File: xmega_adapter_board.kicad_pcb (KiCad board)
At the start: 2 copper layers, 31 x 72.4 mm, 17 parts, among them J1 Conn_01x04, J2 Conn_01x08, J3 Conn_01x08, J4 Conn_01x04, J5 Conn_01x08, J6 Conn_01x08, J7 Conn_01x08, J8 Conn_01x08, U1 ATxmega256D3-AU

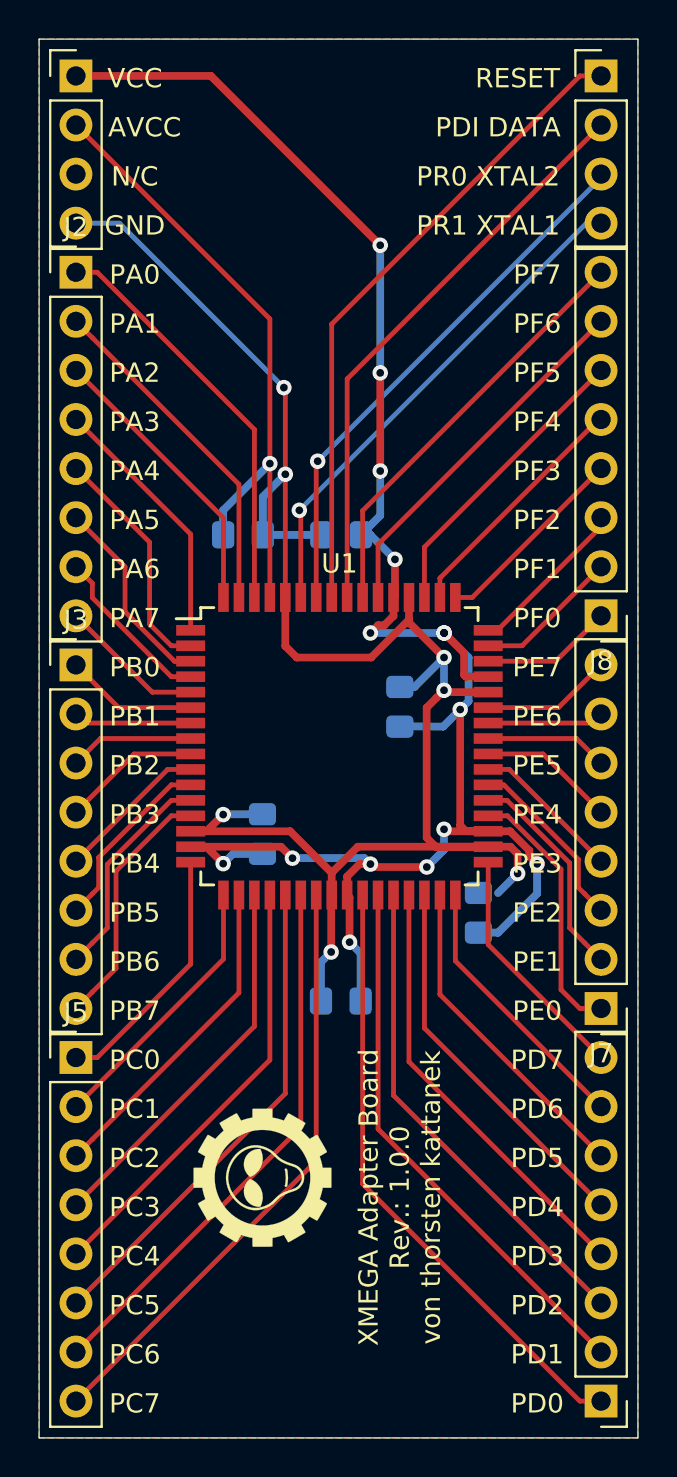
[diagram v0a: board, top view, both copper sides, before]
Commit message: Power LED als rote SMD LED hinzugefuegt
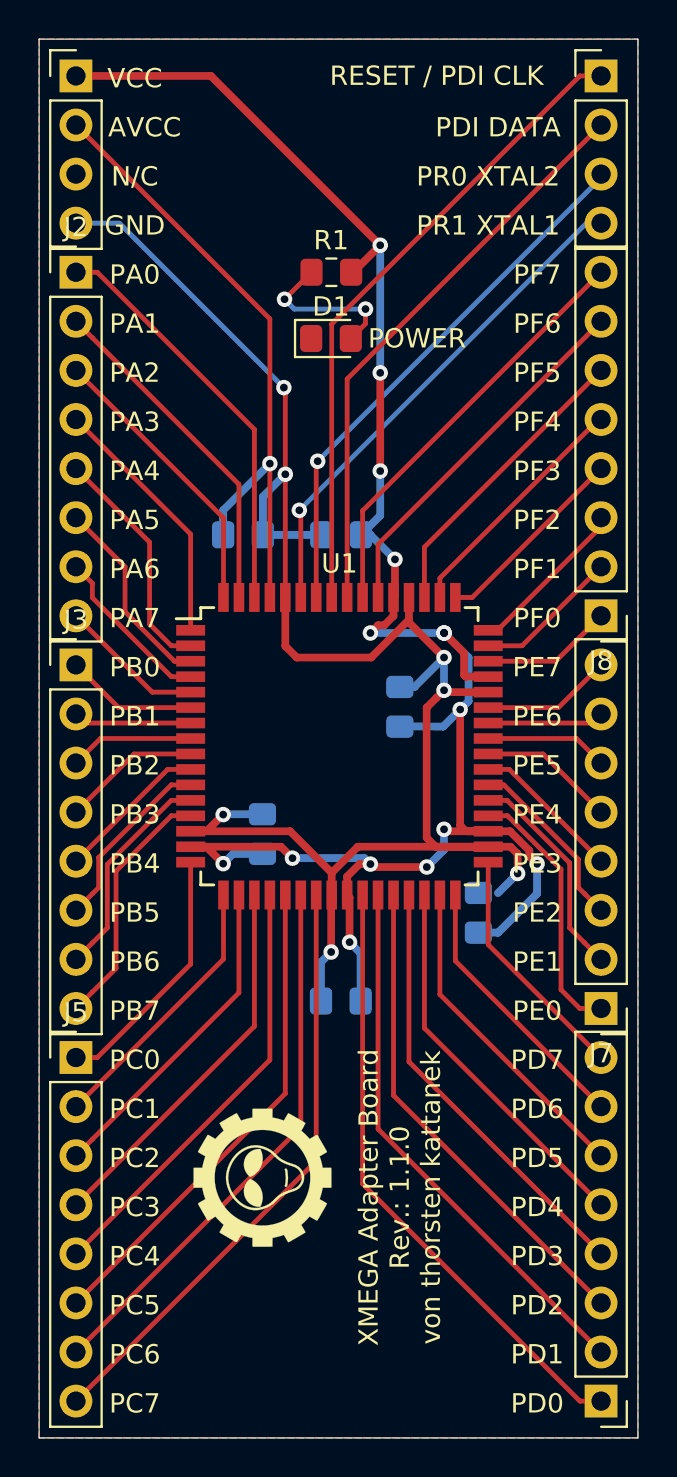
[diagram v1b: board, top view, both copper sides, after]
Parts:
- added D1: LED ROT (2,0V / 20mA), LED_SMD:LED_0805_2012Metric_Pad1.15x1.40mm_HandSolder, F.Cu at (201.2, 80.0)
- added R1: 68, Resistor_SMD:R_0805_2012Metric_Pad1.15x1.40mm_HandSolder, F.Cu at (201.2, 76.6)
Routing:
- net Net-(D1-Pad2): track 0.00 -> 8.22 mm, vias 0 -> 2
- net VCC: track 103.9 -> 106.0 mm
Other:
- board text added: "POWER"
- board text added: "RESET / PDI CLK"
- board text added: "XMEGA Adapter Board Rev.: 1.1.0 von thorsten kattanek"
- board text removed: "XMEGA Adapter Board Rev.: 1.0.0 von thorsten kattanek"
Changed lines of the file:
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@@
   (general
     (thickness 1.6)
-    (drawings 118)
-    (tracks 271)
+    (drawings 119)
+    (tracks 280)
     (zones 0)
-    (modules 17)
-    (nets 57)
+    (modules 19)
+    (nets 58)
   )
   (page A4)
   (title_block
     (title "XMEGA Adapter Board")
-    (date 2020-06-24)
-    (rev 1.0.0)
+    (date 2020-07-12)
+    (rev 1.1.0)
     (comment 1 "Erstellt von: Thorsten Kattanek")
   )
   (layers
     (0 F.Cu signal)
-    (31 B.Cu signal hide)
+    (31 B.Cu signal)
     (32 B.Adhes user hide)
     (33 F.Adhes user hide)
@@
   (net 55 PF0)
   (net 56 "Net-(J1-Pad3)")
+  (net 57 "Net-(D1-Pad2)")
   (net_class Default "Dies ist die voreingestellte Netzklasse."
     (clearance 0.15)
@@
     (uvia_dia 0.3)
     (uvia_drill 0.1)
+    (add_net "Net-(D1-Pad2)")
     (add_net "Net-(J1-Pad3)")
     (add_net PA0)
@@
     (add_net GND)
     (add_net VCC)
+  )
+  (module Resistor_SMD:R_0805_2012Metric_Pad1.15x1.40mm_HandSolder (layer F.Cu)
+    (at 201.177 76.581)
+    (descr "Resistor SMD 0805 (2012 Metric), square (rectangular) end terminal, IPC_7351 nominal with elongated pad for handsoldering. (Body size source: https://docs.google.com/spreadsheets/d/1BsfQQcO9C6DZCsRaXUlFlo91Tg2WpOkGARC1WS5S8t0/edit?usp=sharing), generated with kicad-footprint-generator")
+    (tags "resistor handsolder")
+    (attr smd)
+    (fp_text reference R1 (at -0.009 -1.651) (layer F.SilkS)
+      (effects (font (size 1 1) (thickness 0.15)))
+    )
+    (fp_text value 68 (at 0 1.65) (layer F.Fab)
+      (effects (font (size 1 1) (thickness 0.15)))
+    )
+    (fp_text user %R (at 0 0) (layer F.Fab)
+      (effects (font (size 0.5 0.5) (thickness 0.08)))
+    )
+    (fp_line (start 1.85 0.95) (end -1.85 0.95) (layer F.CrtYd) (width 0.05))
+    (fp_line (start 1.85 -0.95) (end 1.85 0.95) (layer F.CrtYd) (width 0.05))
+    (fp_line (start -1.85 -0.95) (end 1.85 -0.95) (layer F.CrtYd) (width 0.05))
+    (fp_line (start -1.85 0.95) (end -1.85 -0.95) (layer F.CrtYd) (width 0.05))
+    (fp_line (start -0.261252 0.71) (end 0.261252 0.71) (layer F.SilkS) (width 0.12))
+    (fp_line (start -0.261252 -0.71) (end 0.261252 -0.71) (layer F.SilkS) (width 0.12))
+    (fp_line (start 1 0.6) (end -1 0.6) (layer F.Fab) (width 0.1))
+    (fp_line (start 1 -0.6) (end 1 0.6) (layer F.Fab) (width 0.1))
+    (fp_line (start -1 -0.6) (end 1 -0.6) (layer F.Fab) (width 0.1))
+    (fp_line (start -1 0.6) (end -1 -0.6) (layer F.Fab) (width 0.1))
+    (pad 2 smd roundrect (at 1.025 0) (size 1.15 1.4) (layers F.Cu F.Paste F.Mask) (roundrect_rratio 0.217391)
+      (net 7 VCC))
+    (pad 1 smd roundrect (at -1.025 0) (size 1.15 1.4) (layers F.Cu F.Paste F.Mask) (roundrect_rratio 0.217391)
+      (net 57 "Net-(D1-Pad2)"))
+    (model ${KISYS3DMOD}/Resistor_SMD.3dshapes/R_0805_2012Metric.wrl
+      (at (xyz 0 0 0))
+      (scale (xyz 1 1 1))
+      (rotate (xyz 0 0 0))
+    )
+  )
+  (module LED_SMD:LED_0805_2012Metric_Pad1.15x1.40mm_HandSolder (layer F.Cu)
+    (at 201.159 80.01)
+    (descr "LED SMD 0805 (2012 Metric), square (rectangular) end terminal, IPC_7351 nominal, (Body size source: https://docs.google.com/spreadsheets/d/1BsfQQcO9C6DZCsRaXUlFlo91Tg2WpOkGARC1WS5S8t0/edit?usp=sharing), generated with kicad-footprint-generator")
+    (tags "LED handsolder")
+    (attr smd)
+    (fp_text reference D1 (at 0 -1.65) (layer F.SilkS)
+      (effects (font (size 1 1) (thickness 0.15)))
+    )
+    (fp_text value "LED ROT (2,0V / 20mA)" (at 0 1.65) (layer F.Fab)
+      (effects (font (size 1 1) (thickness 0.15)))
+    )
+    (fp_text user %R (at 0 0) (layer F.Fab)
+      (effects (font (size 0.5 0.5) (thickness 0.08)))
+    )
+    (fp_line (start 1.85 0.95) (end -1.85 0.95) (layer F.CrtYd) (width 0.05))
+    (fp_line (start 1.85 -0.95) (end 1.85 0.95) (layer F.CrtYd) (width 0.05))
+    (fp_line (start -1.85 -0.95) (end 1.85 -0.95) (layer F.CrtYd) (width 0.05))
+    (fp_line (start -1.85 0.95) (end -1.85 -0.95) (layer F.CrtYd) (width 0.05))
+    (fp_line (start -1.86 0.96) (end 1 0.96) (layer F.SilkS) (width 0.12))
+    (fp_line (start -1.86 -0.96) (end -1.86 0.96) (layer F.SilkS) (width 0.12))
+    (fp_line (start 1 -0.96) (end -1.86 -0.96) (layer F.SilkS) (width 0.12))
+    (fp_line (start 1 0.6) (end 1 -0.6) (layer F.Fab) (width 0.1))
+    (fp_line (start -1 0.6) (end 1 0.6) (layer F.Fab) (width 0.1))
+    (fp_line (start -1 -0.3) (end -1 0.6) (layer F.Fab) (width 0.1))
+    (fp_line (start -0.7 -0.6) (end -1 -0.3) (layer F.Fab) (width 0.1))
+    (fp_line (start 1 -0.6) (end -0.7 -0.6) (layer F.Fab) (width 0.1))
+    (pad 2 smd roundrect (at 1.025 0) (size 1.15 1.4) (layers F.Cu F.Paste F.Mask) (roundrect_rratio 0.217391)
+      (net 57 "Net-(D1-Pad2)"))
+    (pad 1 smd roundrect (at -1.025 0) (size 1.15 1.4) (layers F.Cu F.Paste F.Mask) (roundrect_rratio 0.217391)
+      (net 1 GND))
+    (model ${KISYS3DMOD}/LED_SMD.3dshapes/LED_0805_2012Metric.wrl
+      (at (xyz 0 0 0))
+      (scale (xyz 1 1 1))
+      (rotate (xyz 0 0 0))
+    )
   )
   (module logos_tk:logo_01_10_7mm_fsilk (layer B.Cu)
@@
     )
   )
+  (gr_text POWER (at 205.613 80.01) (layer F.SilkS)
+    (effects (font (size 1 1) (thickness 0.15)))
+  )
   (gr_text PC7 (at 191.008 135.128) (layer B.SilkS)
     (effects (font (size 1 1) (thickness 0.15)) (justify mirror))
@@
     (effects (font (size 1 1) (thickness 0.15)) (justify mirror))
   )
-  (gr_text "XMEGA Adapter Board\nRev.: 1.0.0\nvon thorsten kattanek" (at 204.724 124.46 90) (layer F.SilkS)
+  (gr_text "XMEGA Adapter Board\nRev.: 1.1.0\nvon thorsten kattanek" (at 204.724 124.46 90) (layer F.SilkS)
     (effects (font (size 1 1) (thickness 0.15)))
   )
@@
     (effects (font (size 1 1) (thickness 0.15)))
   )
-  (gr_text RESET (at 210.82 66.548) (layer F.SilkS)
+  (gr_text "RESET / PDI CLK" (at 206.629 66.421) (layer F.SilkS)
     (effects (font (size 1 1) (thickness 0.15)))
   )
@@
   (segment (start 209.795 110.753) (end 208.788 110.753) (width 0.4) (layer B.Cu) (net 7))
   (segment (start 209.804 110.762) (end 209.795 110.753) (width 0.4) (layer B.Cu) (net 7))
+  (segment (start 202.311 76.581) (end 203.708 75.184) (width 0.4) (layer F.Cu) (net 7))
+  (segment (start 202.202 76.581) (end 202.311 76.581) (width 0.4) (layer F.Cu) (net 7))
   (segment (start 191.91 98.311) (end 187.96 94.361) (width 0.25) (layer F.Cu) (net 8))
   (segment (start 193.896 98.311) (end 191.91 98.311) (width 0.25) (layer F.Cu) (net 8))
@@
   (segment (start 212.788 96.711) (end 215.138 94.361) (width 0.25) (layer F.Cu) (net 55))
   (segment (start 209.296 96.711) (end 212.788 96.711) (width 0.25) (layer F.Cu) (net 55))
+  (via (at 198.755 77.978) (size 0.8) (drill 0.4) (layers F.Cu B.Cu) (net 57))
+  (segment (start 200.152 76.581) (end 198.755 77.978) (width 0.25) (layer F.Cu) (net 57))
+  (via (at 202.946 78.486) (size 0.8) (drill 0.4) (layers F.Cu B.Cu) (net 57))
+  (segment (start 198.755 77.978) (end 199.263 78.486) (width 0.25) (layer B.Cu) (net 57))
+  (segment (start 199.263 78.486) (end 202.946 78.486) (width 0.25) (layer B.Cu) (net 57))
+  (segment (start 202.946 79.248) (end 202.184 80.01) (width 0.25) (layer F.Cu) (net 57))
+  (segment (start 202.946 78.486) (end 202.946 79.248) (width 0.25) (layer F.Cu) (net 57))
   (zone (net 1) (net_name GND) (layer B.Cu) (hatch edge 0.508)
     (connect_pads (clearance 0.508))

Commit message: changed board to version 1.1.0 - added a 3.3 voltage regulator and a reset button
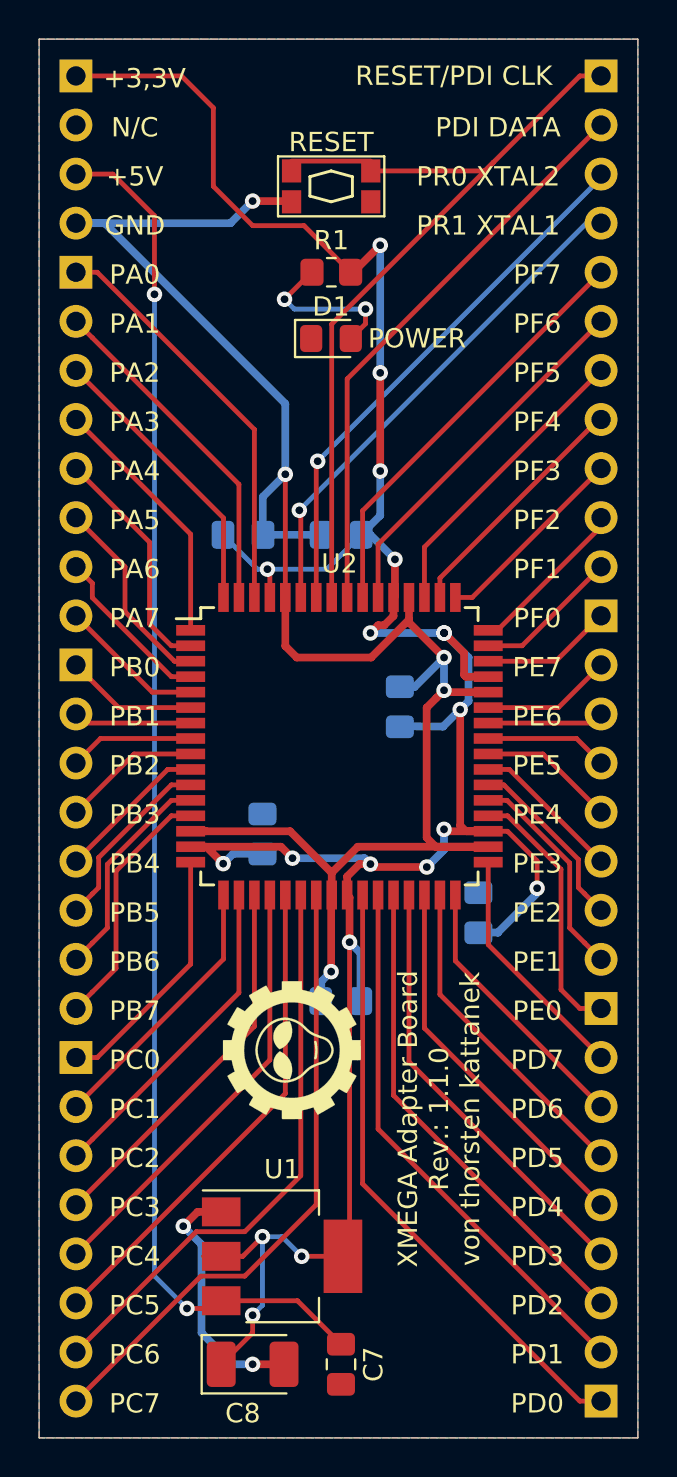
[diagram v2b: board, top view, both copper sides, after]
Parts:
- added C7: 100n, Capacitor_SMD:C_0805_2012Metric_Pad1.18x1.45mm_HandSolder, F.Cu at (201.7, 133.1)
- added C8: 22u, Capacitor_Tantalum_SMD:CP_EIA-3528-12_Kemet-T_Pad1.50x2.35mm_HandSolder, F.Cu at (197.1, 133.1)
- added SW1: SW_Push, button_switch_tk:SW_KMR231G, F.Cu at (201.2, 72.1)
- added U1: AMS1117-3.3, Package_TO_SOT_SMD:SOT-223-3_TabPin2, F.Cu at (198.6, 127.5)
- C1, C2, C3, C4, C5, C6: footprint Capacitor_SMD:C_0805_2012Metric_Pad1.15x1.40mm_HandSolder -> Capacitor_SMD:C_0805_2012Metric_Pad1.18x1.45mm_HandSolder
- J1, J2, J3, J4, J5, J6, J7, J8: moved to B.Cu
- R1: footprint Resistor_SMD:R_0805_2012Metric_Pad1.15x1.40mm_HandSolder -> Resistor_SMD:R_0805_2012Metric_Pad1.20x1.40mm_HandSolder
- moved G*** 6.78 mm to (199.1, 116.8)
- turned J1 to 180 degrees
- turned J2 to 180 degrees
- turned J3 to 180 degrees
- turned J4 to 180 degrees
- turned J5 to 180 degrees
- turned J6 to 0 degrees
- turned J7 to 0 degrees
- turned J8 to 0 degrees
- renumbered U1 to U2
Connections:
- C1 pad 1: VCC -> +3V3
- C2 pad 1: VCC -> +3V3
- C3 pad 1: VCC -> +3V3
- C4 pad 1: VCC -> +3V3
- C5 pad 1: VCC -> +3V3
- C6 pad 1: AVCC -> +3V3
- J1 pad 1: VCC -> +3V3
- J1 pad 2: AVCC -> Net-(J1-Pad2)
- J1 pad 3: Net-(J1-Pad3) -> +5V
- R1 pad 2: VCC -> +3V3
- U2 pad 15: VCC -> +3V3
- U2 pad 25: VCC -> +3V3
- U2 pad 35: VCC -> +3V3
- U2 pad 45: VCC -> +3V3
- U2 pad 53: VCC -> +3V3
- U2 pad 61: AVCC -> +3V3
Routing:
- net +3V3: track 0.00 -> 149.2 mm, vias 0 -> 19
- net VCC: track 106.0 -> 0.00 mm, vias 15 -> 0
- net +5V: track 0.00 -> 71.3 mm, vias 0 -> 2
- net AVCC: track 33.3 -> 0.00 mm, vias 1 -> 0
- net GND: track 95.9 -> 112.8 mm
- net RESET: track 33.4 -> 44.0 mm
- net PC6: track 28.5 -> 29.9 mm
- net PC7: track 31.3 -> 32.7 mm
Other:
- board text added: "+3,3V"
- board text added: "+5V"
- board text added: "RESET/PDI CLK"
- board text removed: "AVCC"
- board text removed: "RESET / PDI CLK"
- board text removed: "VCC"

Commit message: changed to rev 1.2.0
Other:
- board text added: "XMEGA Adapter Board Rev.: 1.2.0 von thorsten kattanek"
- board text removed: "XMEGA Adapter Board Rev.: 1.1.0 von thorsten kattanek"

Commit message: added kicat logo to pcb
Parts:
- added REF**: KiCad-Logo2_5mm_SilkScreen, Symbol:KiCad-Logo2_5mm_SilkScreen, F.Cu at (201.4, 85.6)
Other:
- board text added: "XMEGA Adapter Board Rev.: 1.2.1 von thorsten kattanek"
- board text removed: "XMEGA Adapter Board Rev.: 1.2.0 von thorsten kattanek"
